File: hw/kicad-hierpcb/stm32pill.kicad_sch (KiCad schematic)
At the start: 62 parts, among them SW1 Tactile Switch, SW2 Tactile Switch, U1 3.3V Voltage Regulator 200mA, X1 Crystal 12MHz X322512MSB4SI

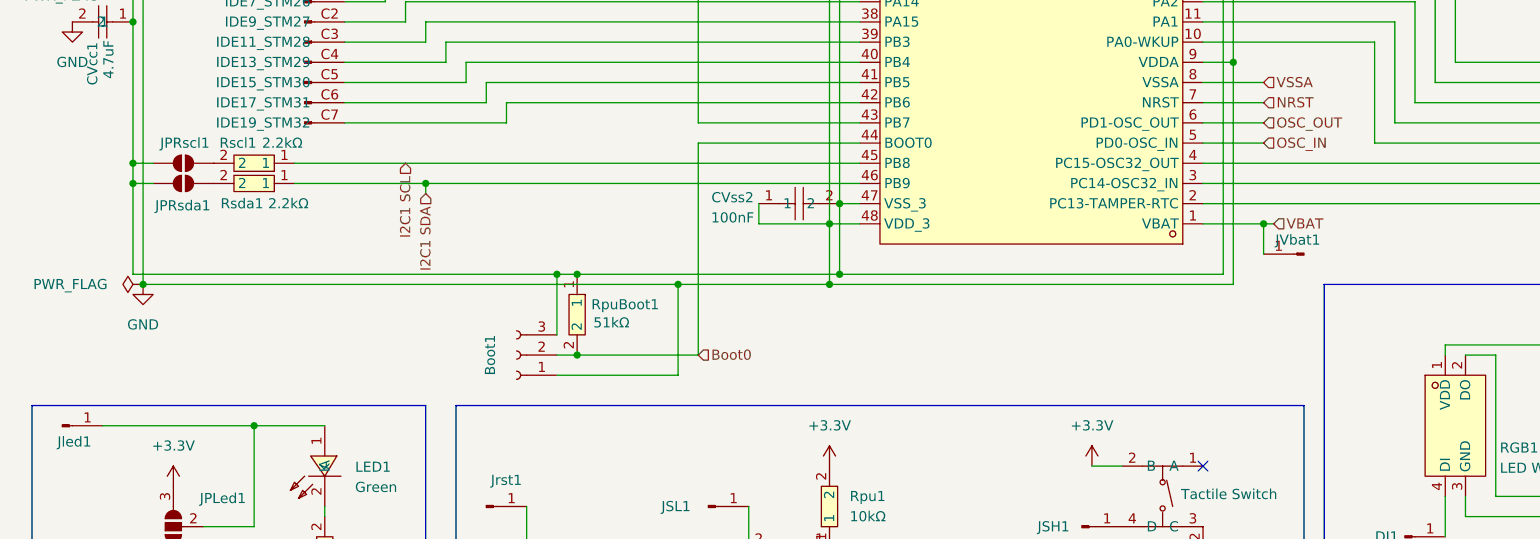
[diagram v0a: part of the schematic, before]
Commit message: boot0: pullDown + serial resistor
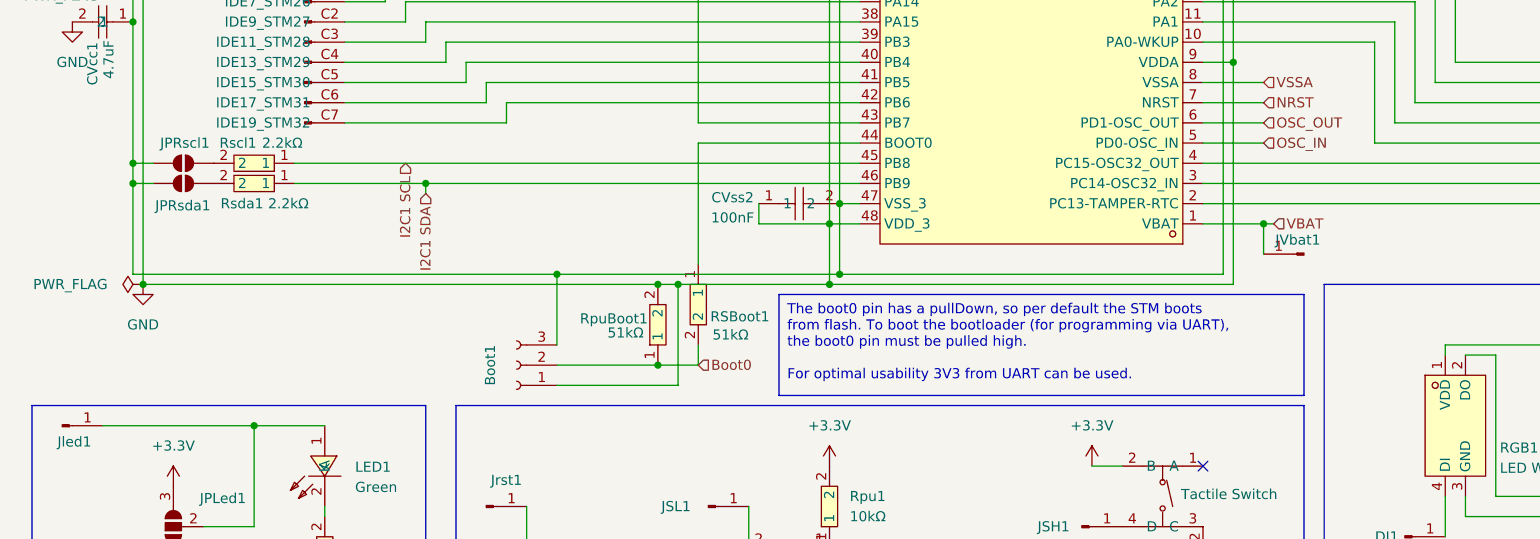
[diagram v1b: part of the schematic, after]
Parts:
- added RSBoot1: 51kΩ, jlcpcb:R0402, symbol jlcpcb:Resistor 51kΩ 0402WGF5102TCE
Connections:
- net +3.3V: no longer RpuBoot1.1
- net Boot0: now also RpuBoot1.1, RSBoot1.2; no longer MCU1.44 (BOOT0), RpuBoot1.2
- net GND: now also RpuBoot1.2
- new net: MCU1.44 (BOOT0), RSBoot1.1
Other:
- moved on the sheet: Boot1
